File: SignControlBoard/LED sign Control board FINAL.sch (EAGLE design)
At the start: 48 parts, among them IC1 MSGEQ7DIL, U1 ATMEGA328P, U2 M5205 5v, Y1 16MHz

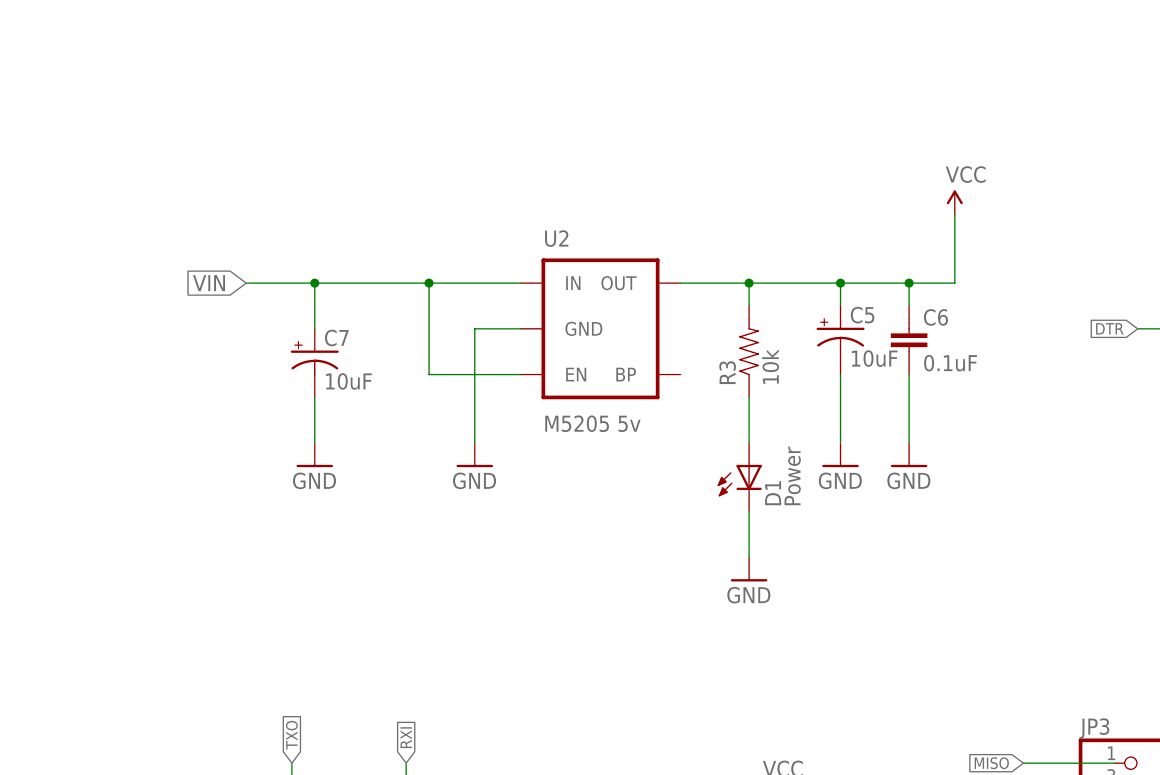
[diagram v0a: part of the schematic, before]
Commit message: Updated control and sign boards. Removed old versions
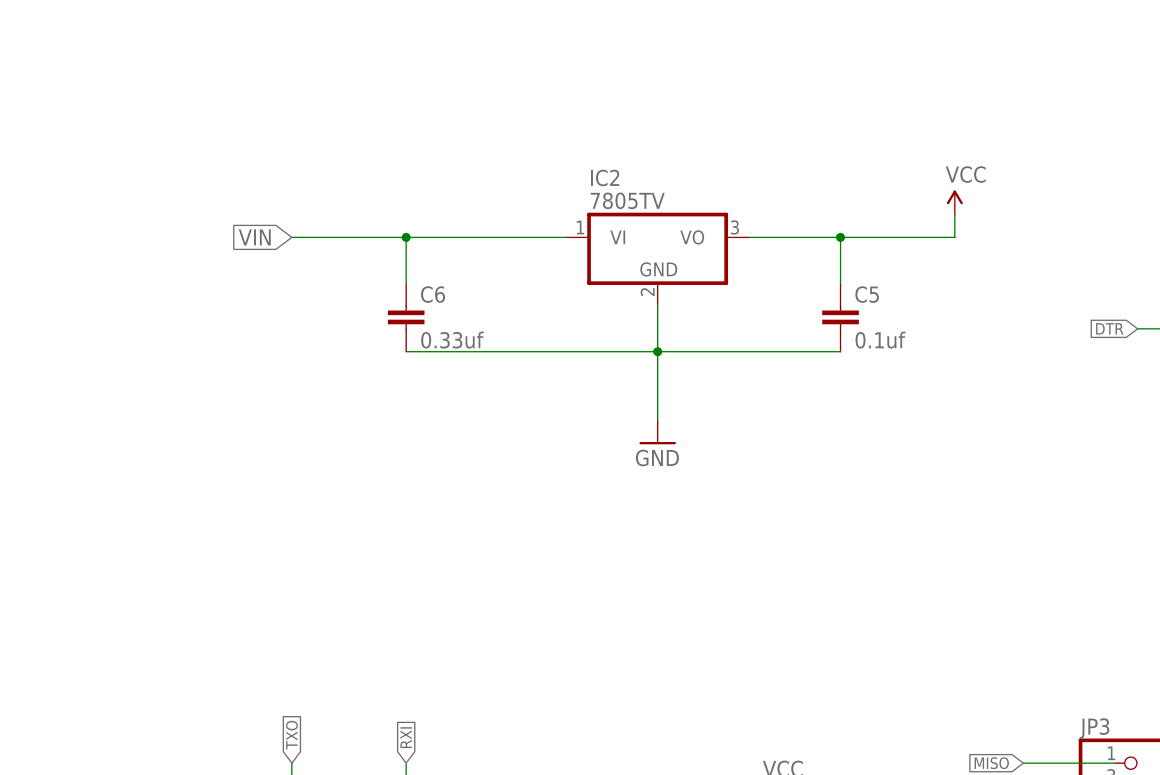
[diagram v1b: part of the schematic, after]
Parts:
- removed C7: 10uF, SparkFun-Passives:CAP_POL1206
- removed D1: Power, SparkFun-LED:LED-RED0603
- removed R3: 10k, SparkFun-Passives:RESISTOR0603-RES
- removed U2: M5205 5v, SparkFun-PowerIC:MIC52055V
- added IC2: 7805TV, linear:7805TV
- C5: value 10uF -> 0.1uf; device SparkFun-Passives:CAP_POL1206 -> capacitor-wima:C2,5-3
- C6: value 0.1uF -> 0.33uf; device SparkFun-Passives:CAP0603-CAP -> capacitor-wima:C2,5-3
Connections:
- removed net N$3: D1.A, R3.1
- net GND: now also C5.2, IC2.GND; no longer C5.-, C7.-, D1.C, U2.GND
- net VCC: now also C5.1, IC2.VO; no longer C5.+, C6.1, R3.2, U2.OUT
- net VIN: now also C6.1, IC2.VI; no longer C7.+, U2.EN, U2.IN
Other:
- moved on the sheet: C6
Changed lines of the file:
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@@
 <part name="GND5" library="SparkFun-Aesthetics" deviceset="GND" device=""/>
 <part name="SUPPLY3" library="SparkFun-Aesthetics" deviceset="VCC" device=""/>
-<part name="U2" library="SparkFun-PowerIC" deviceset="MIC5205" device="5V" value="M5205 5v"/>
-<part name="GND6" library="SparkFun-Aesthetics" deviceset="GND" device=""/>
-<part name="GND7" library="SparkFun-Aesthetics" deviceset="GND" device=""/>
-<part name="C5" library="SparkFun-Passives" deviceset="CAP_POL" device="1206" value="10uF"/>
-<part name="C6" library="SparkFun-Passives" deviceset="CAP" device="0603-CAP" value="0.1uF"/>
-<part name="GND8" library="SparkFun-Aesthetics" deviceset="GND" device=""/>
-<part name="GND9" library="SparkFun-Aesthetics" deviceset="GND" device=""/>
 <part name="SUPPLY4" library="SparkFun-Aesthetics" deviceset="VCC" device=""/>
 <part name="R2" library="SparkFun-Passives" deviceset="RESISTOR" device="0603-RES" value="10k"/>
-<part name="R3" library="SparkFun-Passives" deviceset="RESISTOR" device="0603-RES" value="10k"/>
-<part name="D1" library="SparkFun-LED" deviceset="LED-RED" device="0603" value="Power"/>
-<part name="GND10" library="SparkFun-Aesthetics" deviceset="GND" device=""/>
 <part name="D2" library="SparkFun-LED" deviceset="LED-RED" device="0603" value="D13"/>
 <part name="GND11" library="SparkFun-Aesthetics" deviceset="GND" device=""/>
@@
 <part name="JP2" library="SparkFun-Connectors" deviceset="POWER_JACK" device="PTH"/>
 <part name="SL10" library="con-amp-quick" deviceset="M02" device=""/>
-<part name="C7" library="SparkFun-Passives" deviceset="CAP_POL" device="1206" value="10uF"/>
 <part name="C4" library="capacitor-wima" deviceset="C" device="2,5-3" value="0.01uf"/>
 <part name="C8" library="capacitor-wima" deviceset="C" device="2,5-3" value="0.1uf"/>
@@
 <part name="SL12" library="con-amp-quick" deviceset="M03" device=""/>
 <part name="U$1" library="SparkFun-PowerIC" deviceset="V_REG_LD1117VXX" device=""/>
+<part name="IC2" library="linear" deviceset="78*" device="TV" technology="05"/>
+<part name="C5" library="capacitor-wima" deviceset="C" device="2,5-3" value="0.1uf"/>
+<part name="C6" library="capacitor-wima" deviceset="C" device="2,5-3" value="0.33uf"/>
+<part name="GND6" library="SparkFun-Aesthetics" deviceset="GND" device=""/>
 </parts>
 <sheets>
@@
 <instance part="GND5" gate="1" x="-15.24" y="-5.08"/>
 <instance part="SUPPLY3" gate="G$1" x="-15.24" y="20.32"/>
-<instance part="U2" gate="G$1" x="-33.02" y="73.66"/>
-<instance part="GND6" gate="1" x="-48.26" y="58.42"/>
-<instance part="GND7" gate="1" x="-66.04" y="58.42"/>
-<instance part="C5" gate="G$1" x="-7.62" y="73.66"/>
-<instance part="C6" gate="G$1" x="0" y="71.12"/>
-<instance part="GND8" gate="1" x="-7.62" y="58.42"/>
-<instance part="GND9" gate="1" x="0" y="58.42"/>
 <instance part="SUPPLY4" gate="G$1" x="5.08" y="86.36"/>
 <instance part="R2" gate="G$1" x="142.24" y="2.54" rot="R90"/>
-<instance part="R3" gate="G$1" x="-17.78" y="71.12" rot="R90"/>
-<instance part="D1" gate="G$1" x="-17.78" y="58.42"/>
-<instance part="GND10" gate="1" x="-17.78" y="45.72"/>
 <instance part="D2" gate="G$1" x="142.24" y="-10.16"/>
 <instance part="GND11" gate="1" x="142.24" y="-22.86"/>
@@
 <instance part="JP2" gate="G$1" x="-35.56" y="-27.94" rot="R180"/>
 <instance part="SL10" gate="G$1" x="-50.8" y="-45.72" rot="R90"/>
-<instance part="C7" gate="G$1" x="-66.04" y="71.12"/>
 <instance part="C4" gate="G$1" x="198.12" y="76.2"/>
 <instance part="C8" gate="G$1" x="215.9" y="53.34"/>
@@
 <instance part="SL12" gate="G$1" x="165.1" y="157.48" rot="R270"/>
 <instance part="U$1" gate="G$1" x="231.14" y="22.86"/>
+<instance part="IC2" gate="A1" x="-27.94" y="83.82"/>
+<instance part="C5" gate="G$1" x="-7.62" y="76.2"/>
+<instance part="C6" gate="G$1" x="-55.88" y="76.2"/>
+<instance part="GND6" gate="1" x="-27.94" y="60.96"/>
 </instances>
 <busses>
@@
 <pinref part="GND5" gate="1" pin="GND"/>
 <wire x1="-15.24" y1="5.08" x2="-15.24" y2="-2.54" width="0.1524" layer="91"/>
-</segment>
-<segment>
-<pinref part="U2" gate="G$1" pin="GND"/>
-<wire x1="-43.18" y1="73.66" x2="-48.26" y2="73.66" width="0.1524" layer="91"/>
-<wire x1="-48.26" y1="73.66" x2="-48.26" y2="60.96" width="0.1524" layer="91"/>
-<pinref part="GND6" gate="1" pin="GND"/>
-</segment>
-<segment>
-<wire x1="-66.04" y1="66.04" x2="-66.04" y2="60.96" width="0.1524" layer="91"/>
-<pinref part="GND7" gate="1" pin="GND"/>
-<pinref part="C7" gate="G$1" pin="-"/>
-</segment>
-<segment>
-<pinref part="C5" gate="G$1" pin="-"/>
-<wire x1="-7.62" y1="68.58" x2="-7.62" y2="60.96" width="0.1524" layer="91"/>
-<pinref part="GND8" gate="1" pin="GND"/>
-</segment>
-<segment>
-<pinref part="C6" gate="G$1" pin="2"/>
-<wire x1="0" y1="68.58" x2="0" y2="60.96" width="0.1524" layer="91"/>
-<pinref part="GND9" gate="1" pin="GND"/>
-</segment>
-<segment>
-<pinref part="D1" gate="G$1" pin="C"/>
-<pinref part="GND10" gate="1" pin="GND"/>
-<wire x1="-17.78" y1="53.34" x2="-17.78" y2="48.26" width="0.1524" layer="91"/>
 </segment>
 <segment>
@@
 <label x="226.06" y="15.24" size="1.778" layer="95" rot="R180" xref="yes"/>
 </segment>
+<segment>
+<pinref part="IC2" gate="A1" pin="GND"/>
+<wire x1="-27.94" y1="76.2" x2="-27.94" y2="71.12" width="0.1524" layer="91"/>
+<pinref part="GND6" gate="1" pin="GND"/>
+<pinref part="C6" gate="G$1" pin="2"/>
+<wire x1="-27.94" y1="71.12" x2="-27.94" y2="63.5" width="0.1524" layer="91"/>
+<wire x1="-55.88" y1="71.12" x2="-27.94" y2="71.12" width="0.1524" layer="91"/>
+<junction x="-27.94" y="71.12"/>
+<pinref part="C5" gate="G$1" pin="2"/>
+<wire x1="-7.62" y1="71.12" x2="-27.94" y2="71.12" width="0.1524" layer="91"/>
+</segment>
 </net>
 <net name="VCC" class="0">
@@
 <pinref part="SUPPLY3" gate="G$1" pin="VCC"/>
 <wire x1="-15.24" y1="12.7" x2="-15.24" y2="20.32" width="0.1524" layer="91"/>
-</segment>
-<segment>
-<pinref part="U2" gate="G$1" pin="OUT"/>
-<wire x1="-25.4" y1="78.74" x2="-17.78" y2="78.74" width="0.1524" layer="91"/>
-<wire x1="-17.78" y1="78.74" x2="-7.62" y2="78.74" width="0.1524" layer="91"/>
-<wire x1="-7.62" y1="78.74" x2="0" y2="78.74" width="0.1524" layer="91"/>
-<wire x1="0" y1="78.74" x2="5.08" y2="78.74" width="0.1524" layer="91"/>
-<wire x1="5.08" y1="78.74" x2="5.08" y2="86.36" width="0.1524" layer="91"/>
-<pinref part="C5" gate="G$1" pin="+"/>
-<wire x1="-7.62" y1="76.2" x2="-7.62" y2="78.74" width="0.1524" layer="91"/>
-<junction x="-7.62" y="78.74"/>
-<pinref part="C6" gate="G$1" pin="1"/>
-<wire x1="0" y1="76.2" x2="0" y2="78.74" width="0.1524" layer="91"/>
-<junction x="0" y="78.74"/>
-<pinref part="SUPPLY4" gate="G$1" pin="VCC"/>
-<pinref part="R3" gate="G$1" pin="2"/>
-<wire x1="-17.78" y1="76.2" x2="-17.78" y2="78.74" width="0.1524" layer="91"/>
-<junction x="-17.78" y="78.74"/>
 </segment>
 <segment>
@@
 <label x="220.98" y="22.86" size="1.778" layer="95" rot="R180" xref="yes"/>
 </segment>
+<segment>
+<pinref part="IC2" gate="A1" pin="VO"/>
+<pinref part="SUPPLY4" gate="G$1" pin="VCC"/>
+<wire x1="-17.78" y1="83.82" x2="-7.62" y2="83.82" width="0.1524" layer="91"/>
+<wire x1="-7.62" y1="83.82" x2="5.08" y2="83.82" width="0.1524" layer="91"/>
+<wire x1="5.08" y1="83.82" x2="5.08" y2="86.36" width="0.1524" layer="91"/>
+<wire x1="-7.62" y1="83.82" x2="-7.62" y2="78.74" width="0.1524" layer="91"/>
+<junction x="-7.62" y="83.82"/>
+<pinref part="C5" gate="G$1" pin="1"/>
+</segment>
 </net>
 <net name="RXI" class="0">
@@
 <net name="VIN" class="0">
 <segment>
-<pinref part="U2" gate="G$1" pin="IN"/>
-<wire x1="-43.18" y1="78.74" x2="-53.34" y2="78.74" width="0.1524" layer="91"/>
-<pinref part="U2" gate="G$1" pin="EN"/>
-<wire x1="-53.34" y1="78.74" x2="-66.04" y2="78.74" width="0.1524" layer="91"/>
-<wire x1="-66.04" y1="78.74" x2="-73.66" y2="78.74" width="0.1524" layer="91"/>
-<wire x1="-43.18" y1="68.58" x2="-53.34" y2="68.58" width="0.1524" layer="91"/>
-<wire x1="-53.34" y1="68.58" x2="-53.34" y2="78.74" width="0.1524" layer="91"/>
-<junction x="-53.34" y="78.74"/>
-<label x="-73.66" y="78.74" size="1.778" layer="95" rot="R180" xref="yes"/>
-<wire x1="-66.04" y1="73.66" x2="-66.04" y2="78.74" width="0.1524" layer="91"/>
-<junction x="-66.04" y="78.74"/>
-<pinref part="C7" gate="G$1" pin="+"/>
-</segment>
-<segment>
 <label x="-71.12" y="-38.1" size="1.27" layer="95" rot="R180" xref="yes"/>
 <pinref part="SL10" gate="G$1" pin="2"/>
 <wire x1="-53.34" y1="-38.1" x2="-71.12" y2="-38.1" width="0.1524" layer="91"/>
+</segment>
+<segment>
+<pinref part="IC2" gate="A1" pin="VI"/>
+<wire x1="-38.1" y1="83.82" x2="-55.88" y2="83.82" width="0.1524" layer="91"/>
+<label x="-68.58" y="83.82" size="1.778" layer="95" rot="R180" xref="yes"/>
+<wire x1="-55.88" y1="83.82" x2="-68.58" y2="83.82" width="0.1524" layer="91"/>
+<wire x1="-55.88" y1="83.82" x2="-55.88" y2="78.74" width="0.1524" layer="91"/>
+<junction x="-55.88" y="83.82"/>
+<pinref part="C6" gate="G$1" pin="1"/>
 </segment>
 </net>
@@
 </segment>
 </net>
-<net name="N$3" class="0">
-<segment>
-<pinref part="R3" gate="G$1" pin="1"/>
-<pinref part="D1" gate="G$1" pin="A"/>
-<wire x1="-17.78" y1="66.04" x2="-17.78" y2="60.96" width="0.1524" layer="91"/>
-</segment>
-</net>
